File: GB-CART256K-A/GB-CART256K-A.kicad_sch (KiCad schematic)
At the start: 26 parts

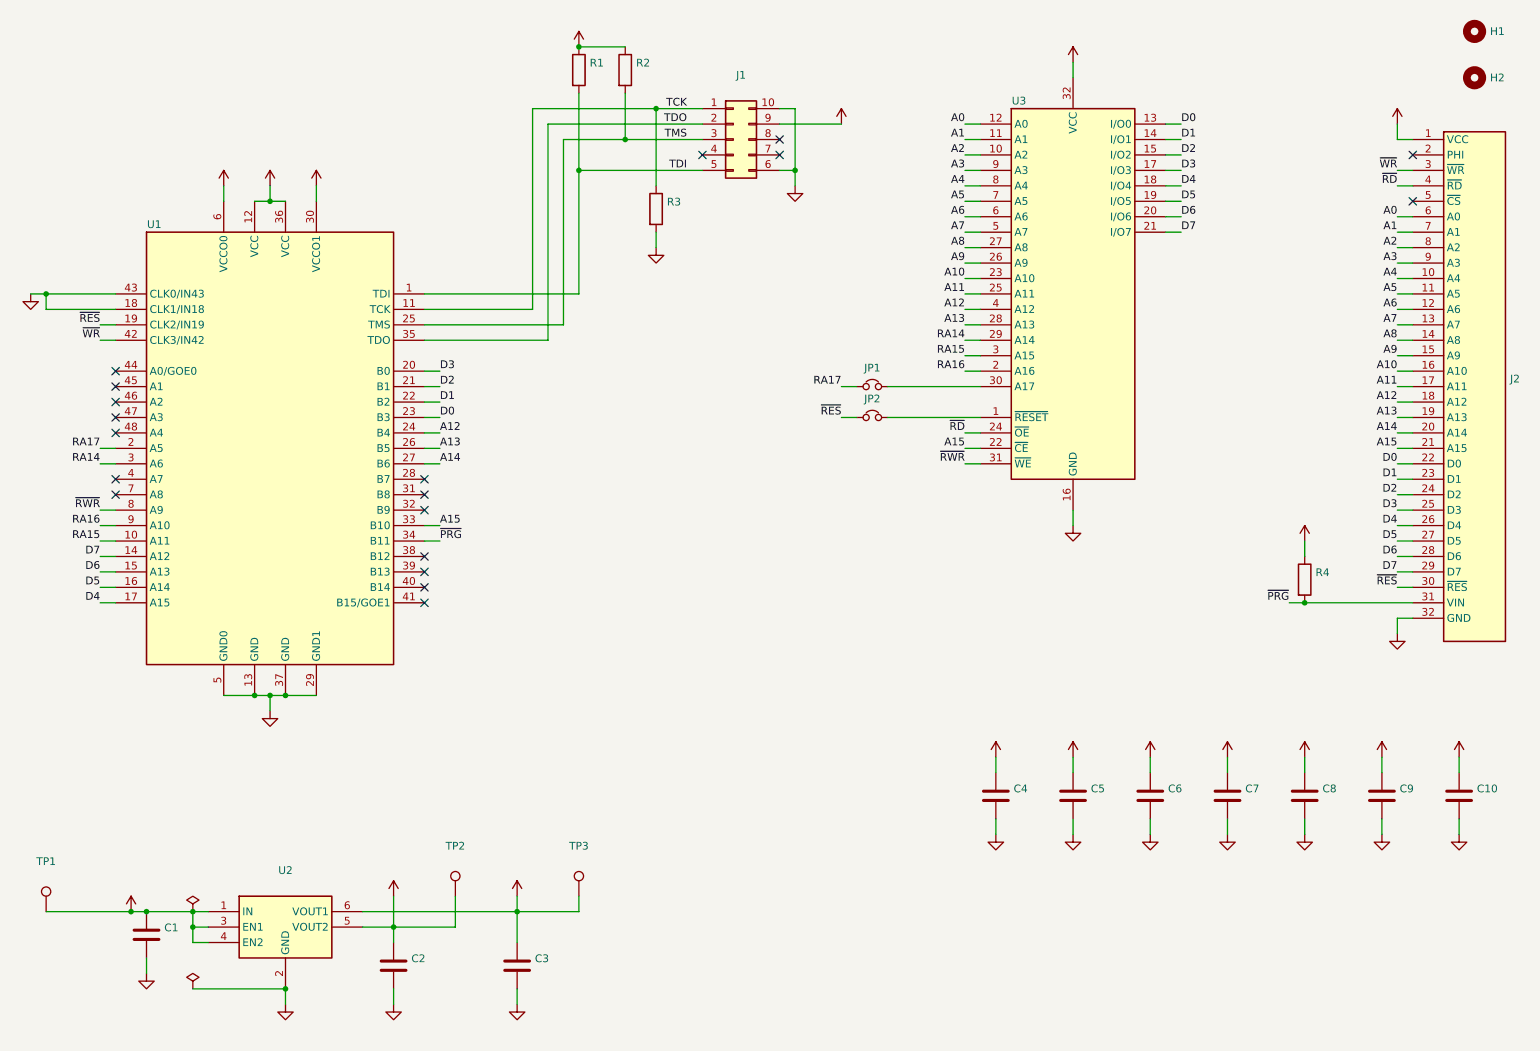
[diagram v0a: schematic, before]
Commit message: Upgrade projects to KiCad 7
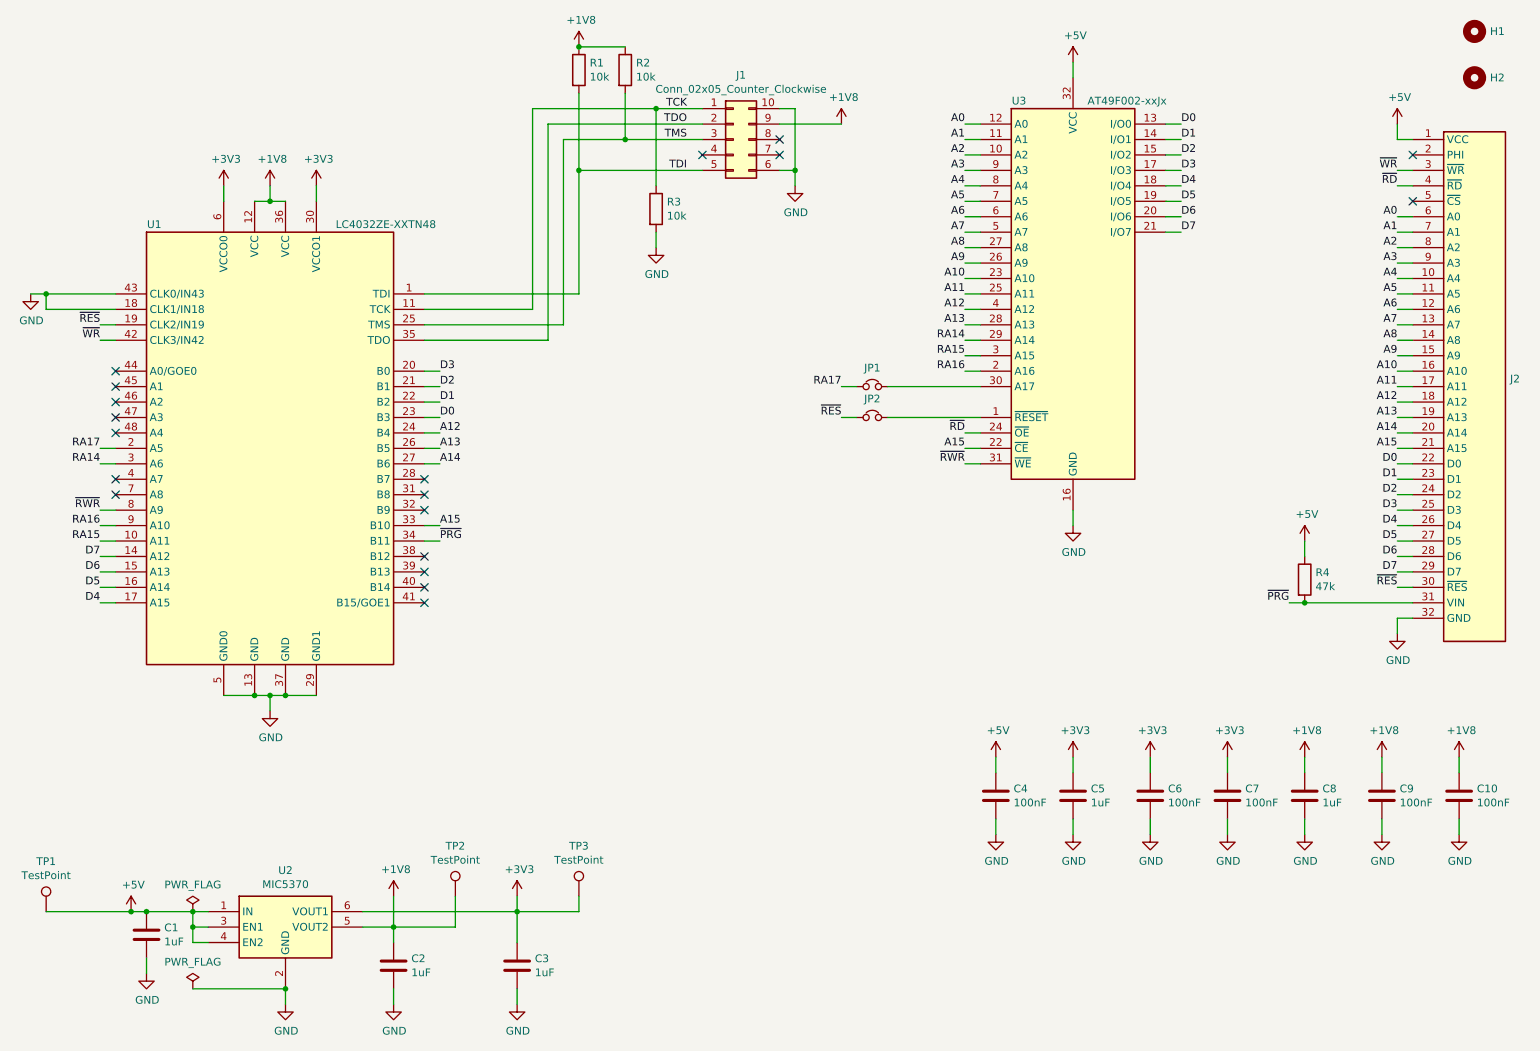
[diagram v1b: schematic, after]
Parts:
- C1, C2, C3, C5, C8: value (none) -> 1uF; footprint (none) -> Capacitor_SMD:C_0805_2012Metric
- C10, C4, C6, C7, C9: value (none) -> 100nF; footprint (none) -> Capacitor_SMD:C_0603_1608Metric
- H1: value (none) -> DNF; footprint (none) -> Gekkio_MountingHole:MountingHole_7.2mm
- H2: value (none) -> DNF; footprint (none) -> Gekkio_MountingHole:MountingHole_2.3mm
- J1: value (none) -> Conn_02x05_Counter_Clockwise; footprint (none) -> Connector:Tag-Connect_TC2050-IDC-NL_2x05_P1.27mm_Vertical
- J2: value (none) -> DNF; footprint (none) -> Gekkio_Connector_PCBEdge:GameBoy_Cartridge_1x32_P1.50mm_Edge
- JP1, JP2: value (none) -> DNF; footprint (none) -> Jumper:SolderJumper-2_P1.3mm_Open_RoundedPad1.0x1.5mm
- R1, R2, R3: value (none) -> 10k; footprint (none) -> Resistor_SMD:R_0603_1608Metric
- R4: value (none) -> 47k; footprint (none) -> Resistor_SMD:R_0603_1608Metric
- TP1, TP2, TP3: value (none) -> TestPoint; footprint (none) -> TestPoint:TestPoint_THTPad_D2.0mm_Drill1.0mm
- U1: value (none) -> LC4032ZE-XXTN48; footprint (none) -> Package_QFP:TQFP-48_7x7mm_P0.5mm
- U2: value (none) -> MIC5370; footprint (none) -> Package_DFN_QFN:MLF-6-1EP_1.6x1.6mm_P0.5mm_EP0.5x1.26mm
- U3: value (none) -> AT49F002-xxJx; footprint (none) -> Package_LCC:PLCC-32_11.4x14.0mm_P1.27mm
